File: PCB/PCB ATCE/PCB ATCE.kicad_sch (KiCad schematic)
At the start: 28 parts, among them J1 USB_OTG, J2 Conn_Coaxial, SW1 SW_Push, SW2 SW_Push, U2 ${SIM.PARAMS}, Y1 16MHz

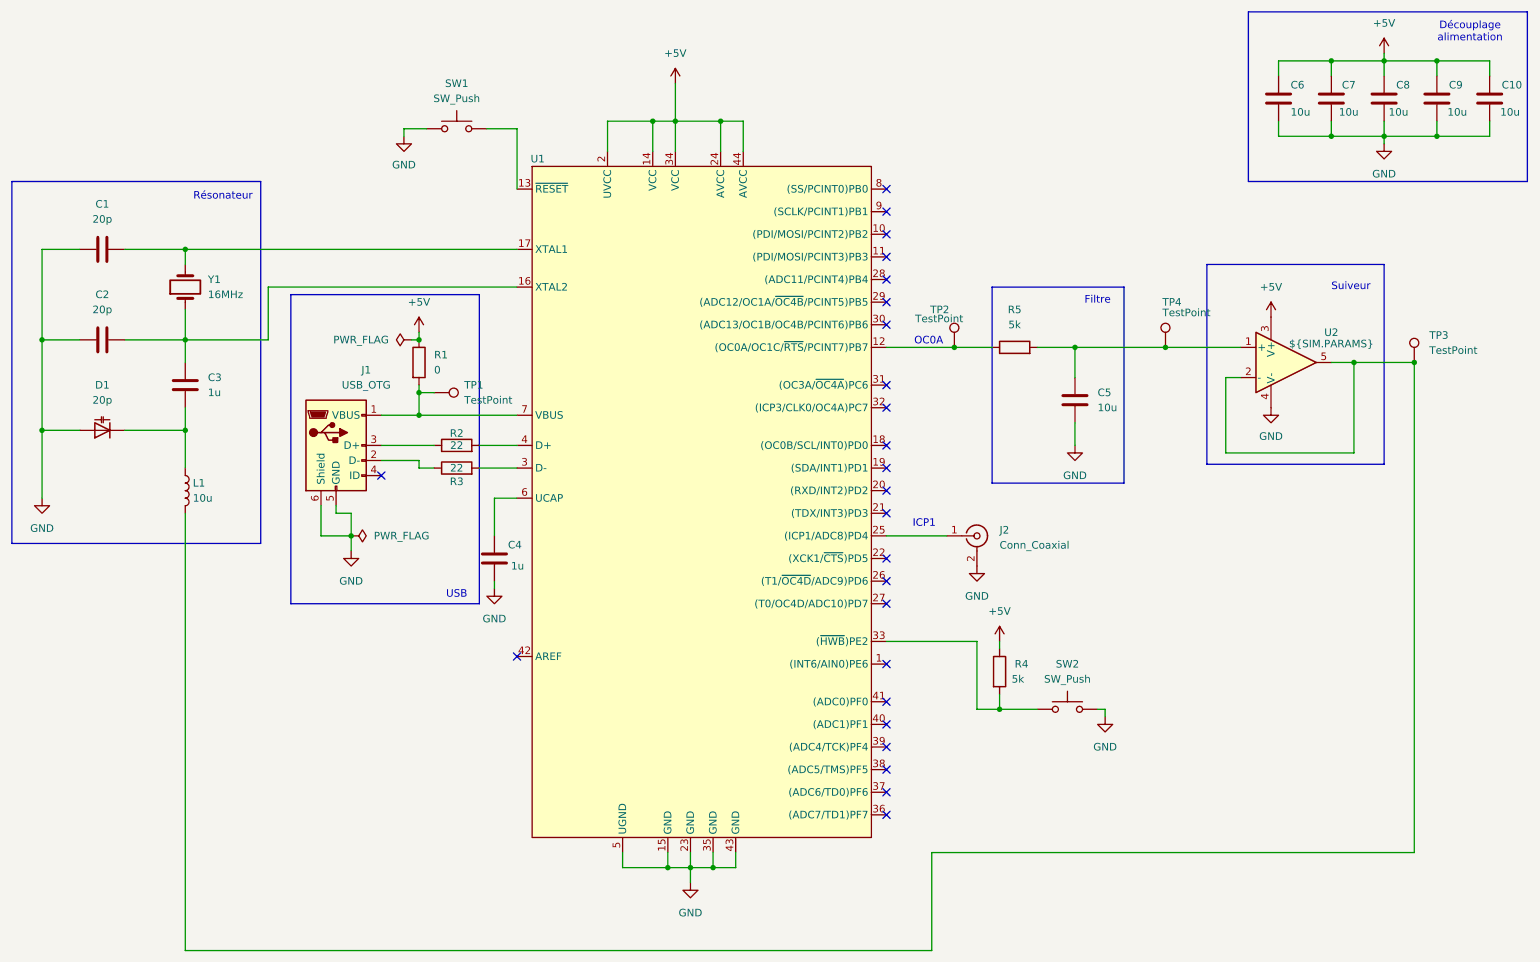
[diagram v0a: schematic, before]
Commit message: Modification des condensateurs de pieds du résonateur et retrait du point de test de l'alimentation
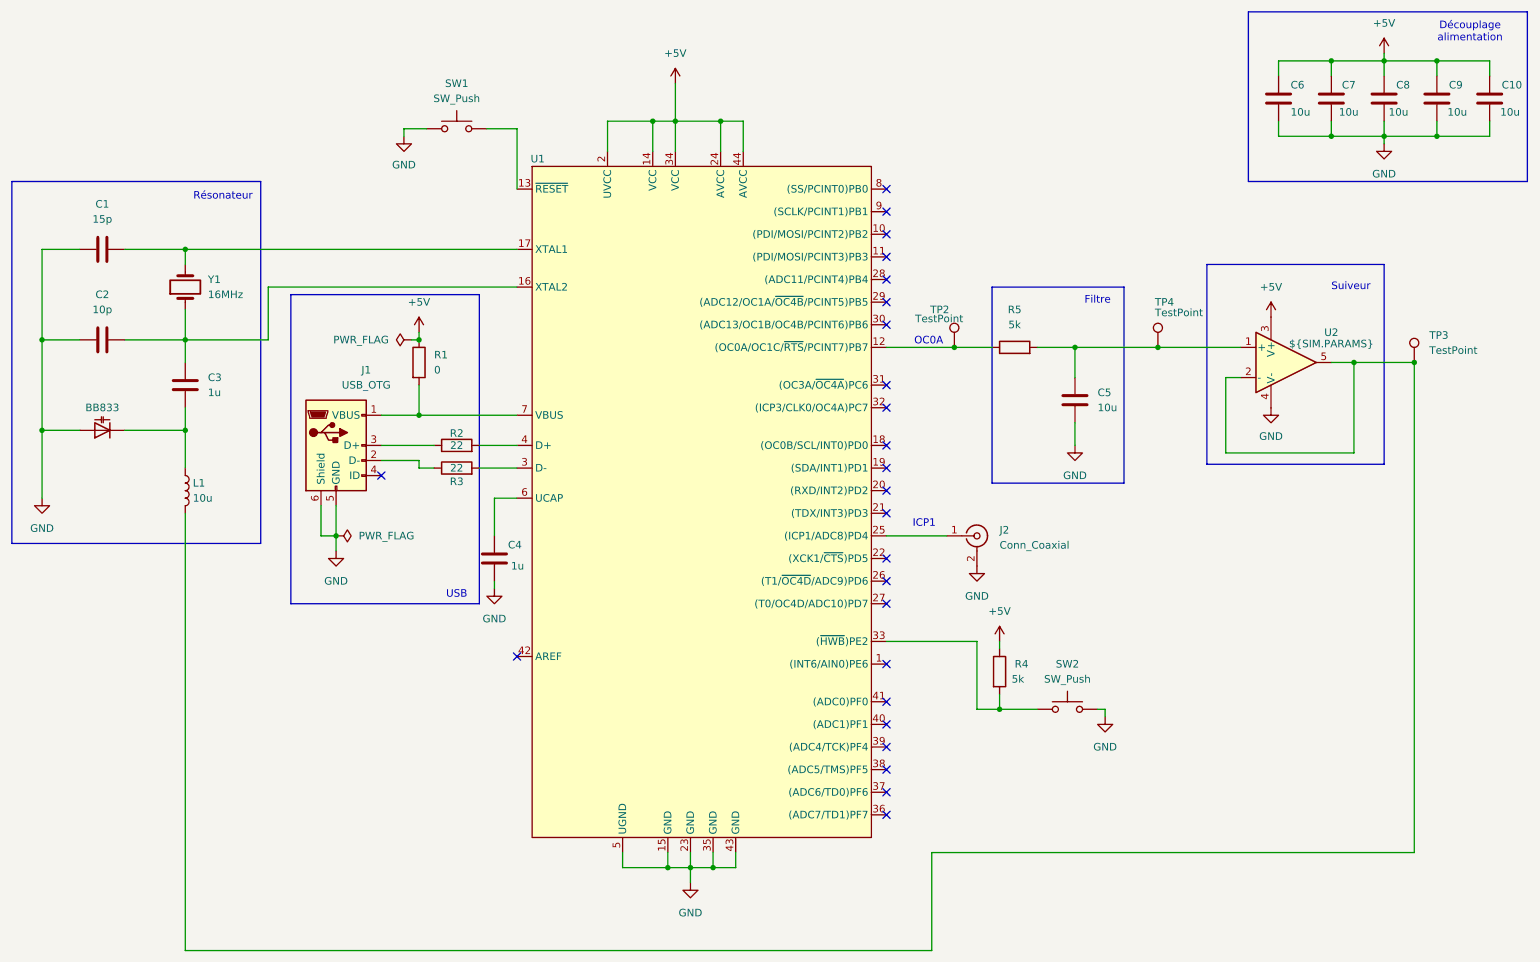
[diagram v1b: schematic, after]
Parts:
- removed TP1: TestPoint, symbol Connector:TestPoint
- BB833: renamed from D1; value 20p -> ~
- C1: value 20p -> 15p
- C2: value 20p -> 10p
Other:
- moved on the sheet: TP4
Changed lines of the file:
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@@
 	)
 	(junction
-		(at 85.09 78.74)
-		(diameter 0)
-		(color 0 0 0 0)
-	)
-	(junction
 		(at 134.62 158.75)
 		(diameter 0)
@@
 	)
 	(junction
-		(at 73.66 102.87)
+		(at 71.12 102.87)
 		(diameter 0)
 		(color 0 0 0 0)
@@
 	)
 	(junction
-		(at 210.82 71.12)
-		(diameter 0)
-		(color 0 0 0 0)
-	)
-	(junction
 		(at 45.72 85.09)
 		(diameter 0)
@@
 	)
 	(junction
+		(at 209.55 71.12)
+		(diameter 0)
+		(color 0 0 0 0)
+	)
+	(junction
 		(at 21.59 85.09)
 		(diameter 0)
@@
 	(wire
 		(pts
+			(xy 71.12 97.79) (xy 71.12 102.87)
+		)
+		(stroke
+			(width 0)
+			(type default)
+		)
+	)
+	(wire
+		(pts
 			(xy 247.65 33.02) (xy 247.65 35.56)
 		)
@@
 	(wire
 		(pts
-			(xy 71.12 99.06) (xy 73.66 99.06)
-		)
-		(stroke
-			(width 0)
-			(type default)
-		)
-	)
-	(wire
-		(pts
 			(xy 138.43 158.75) (xy 138.43 156.21)
 		)
@@
 	(wire
 		(pts
-			(xy 68.58 102.87) (xy 73.66 102.87)
+			(xy 68.58 102.87) (xy 71.12 102.87)
 		)
 		(stroke
@@
 	(wire
 		(pts
-			(xy 85.09 78.74) (xy 85.09 77.47)
-		)
-		(stroke
-			(width 0)
-			(type default)
-		)
-	)
-	(wire
-		(pts
 			(xy 85.09 90.17) (xy 85.09 91.44)
 		)
@@
 	(wire
 		(pts
-			(xy 210.82 71.12) (xy 223.52 71.12)
-		)
-		(stroke
-			(width 0)
-			(type default)
-		)
-	)
-	(wire
-		(pts
-			(xy 71.12 97.79) (xy 71.12 99.06)
-		)
-		(stroke
-			(width 0)
-			(type default)
-		)
-	)
-	(wire
-		(pts
 			(xy 179.07 120.65) (xy 163.83 120.65)
 		)
@@
 	(wire
 		(pts
-			(xy 87.63 78.74) (xy 85.09 78.74)
-		)
-		(stroke
-			(width 0)
-			(type default)
-		)
-	)
-	(wire
-		(pts
 			(xy 45.72 69.85) (xy 45.72 64.77)
 		)
@@
 	(wire
 		(pts
-			(xy 73.66 99.06) (xy 73.66 102.87)
-		)
-		(stroke
-			(width 0)
-			(type default)
-		)
-	)
-	(wire
-		(pts
 			(xy 35.56 54.61) (xy 45.72 54.61)
 		)
@@
 	(wire
 		(pts
-			(xy 195.58 71.12) (xy 210.82 71.12)
+			(xy 195.58 71.12) (xy 209.55 71.12)
 		)
 		(stroke
@@
 	(wire
 		(pts
-			(xy 73.66 102.87) (xy 73.66 105.41)
+			(xy 71.12 102.87) (xy 71.12 105.41)
 		)
 		(stroke
@@
 	(wire
 		(pts
-			(xy 85.09 78.74) (xy 85.09 82.55)
+			(xy 85.09 77.47) (xy 85.09 82.55)
 		)
 		(stroke
@@
 	(wire
 		(pts
+			(xy 209.55 71.12) (xy 223.52 71.12)
+		)
+		(stroke
+			(width 0)
+			(type default)
+		)
+	)
+	(wire
+		(pts
 			(xy 139.7 33.02) (xy 139.7 38.1)
 		)
@@
 			)
 		)
-		(property "Value" "20p"
+		(property "Value" "15p"
 			(at 31.75 49.53 90)
 			(effects
@@
 	(symbol
 		(lib_id "Connector:TestPoint")
-		(at 210.82 71.12 0)
+		(at 209.55 71.12 0)
 		(unit 1)
 		(exclude_from_sim no)
@@
 		(dnp no)
 		(property "Reference" "TP4"
-			(at 210.312 63.5 0)
+			(at 209.042 63.5 0)
 			(effects
 				(font
@@
 		)
 		(property "Value" "TestPoint"
-			(at 210.312 65.278 0)
+			(at 209.042 65.278 0)
 			(effects
 				(font
@@
 		)
 		(property "Footprint" ""
-			(at 215.9 71.12 0)
+			(at 214.63 71.12 0)
 			(effects
 				(font
@@
 		)
 		(property "Datasheet" "~"
-			(at 215.9 71.12 0)
+			(at 214.63 71.12 0)
 			(effects
 				(font
@@
 		)
 		(property "Description" "test point"
-			(at 210.82 71.12 0)
+			(at 209.55 71.12 0)
 			(effects
 				(font
@@
 	)
 	(symbol
-		(lib_id "Connector:TestPoint")
-		(at 87.63 78.74 270)
-		(unit 1)
-		(exclude_from_sim no)
-		(in_bom yes)
-		(on_board yes)
-		(dnp no)
-		(fields_autoplaced yes)
-		(property "Reference" "TP1"
-			(at 92.71 77.4699 90)
-			(effects
-				(font
-					(size 1.27 1.27)
-				)
-				(justify left)
-			)
-		)
-		(property "Value" "TestPoint"
-			(at 92.71 80.0099 90)
-			(effects
-				(font
-					(size 1.27 1.27)
-				)
-				(justify left)
-			)
-		)
-		(property "Footprint" ""
-			(at 87.63 83.82 0)
-			(effects
-				(font
-					(size 1.27 1.27)
-				)
-				(hide yes)
-			)
-		)
-		(property "Datasheet" "~"
-			(at 87.63 83.82 0)
-			(effects
-				(font
-					(size 1.27 1.27)
-				)
-				(hide yes)
-			)
-		)
-		(property "Description" "test point"
-			(at 87.63 78.74 0)
-			(effects
-				(font
-					(size 1.27 1.27)
-				)
-				(hide yes)
-			)
-		)
-		(pin "1"
-		)
-		(instances
-			(project "PCB ATCE"
-				(path "/0ca51401-30cc-4cc1-83e5-abd29d3bd674"
-					(reference "TP1")
-					(unit 1)
-				)
-			)
-		)
-	)
-	(symbol
 		(lib_id "power:+5V")
 		(at 128.27 26.67 0)
@@
 	(symbol
 		(lib_id "power:PWR_FLAG")
-		(at 73.66 102.87 270)
+		(at 71.12 102.87 270)
 		(unit 1)
 		(exclude_from_sim no)
@@
 		(fields_autoplaced yes)
 		(property "Reference" "#FLG01"
-			(at 75.565 102.87 0)
+			(at 73.025 102.87 0)
 			(effects
 				(font
@@
 		)
 		(property "Value" "PWR_FLAG"
-			(at 77.47 102.8699 90)
+			(at 74.93 102.8699 90)
 			(effects
 				(font
@@
 		)
 		(property "Footprint" ""
-			(at 73.66 102.87 0)
+			(at 71.12 102.87 0)
 			(effects
 				(font
@@
 		)
 		(property "Datasheet" "~"
-			(at 73.66 102.87 0)
+			(at 71.12 102.87 0)
 			(effects
 				(font
@@
 		)
 		(property "Description" "Special symbol for telling ERC where power comes from"
-			(at 73.66 102.87 0)
+			(at 71.12 102.87 0)
 			(effects
 				(font
@@
 	(symbol
 		(lib_id "power:GND")
-		(at 73.66 105.41 0)
+		(at 71.12 105.41 0)
 		(unit 1)
 		(exclude_from_sim no)
@@
 		(fields_autoplaced yes)
 		(property "Reference" "#PWR03"
-			(at 73.66 111.76 0)
+			(at 71.12 111.76 0)
 			(effects
 				(font
@@
 		)
 		(property "Value" "GND"
-			(at 73.66 110.49 0)
+			(at 71.12 110.49 0)
 			(effects
 				(font
@@
 		)
 		(property "Footprint" ""
-			(at 73.66 105.41 0)
+			(at 71.12 105.41 0)
 			(effects
 				(font
@@
 		)
 		(property "Datasheet" ""
-			(at 73.66 105.41 0)
+			(at 71.12 105.41 0)
 			(effects
 				(font
@@
 		)
 		(property "Description" "Power symbol creates a global label with name \"GND\" , ground"
-			(at 73.66 105.41 0)
+			(at 71.12 105.41 0)
 			(effects
 				(font
@@
 		(on_board yes)
 		(dnp no)
-		(property "Reference" "D1"
-			(at 31.75 77.47 0)
+		(property "Reference" "BB833"
+			(at 31.75 81.28 0)
 			(effects
 				(font
@@
 			)
 		)
-		(property "Value" "20p"
+		(property "Value" "~"
 			(at 31.75 80.01 0)
 			(effects
@@
 			(project ""
 				(path "/0ca51401-30cc-4cc1-83e5-abd29d3bd674"
-					(reference "D1")
+					(reference "BB833")
 					(unit 1)
 				)
@@
 			)
 		)
-		(property "Value" "20p"
+		(property "Value" "10p"
 			(at 31.75 64.77 90)
 			(effects

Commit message: ajout des empreintes et BOM
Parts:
- BB833: footprint (none) -> Diode_SMD:D_0805_2012Metric_Pad1.15x1.40mm_HandSolder; Prix/U (none) -> 0,172 €
- C1: footprint (none) -> Capacitor_SMD:C_0805_2012Metric_Pad1.18x1.45mm_HandSolder; Prix/U (none) -> 0,0742 €
- C10, C5, C6, C7, C8, C9: footprint (none) -> Capacitor_SMD:C_1206_3216Metric_Pad1.33x1.80mm_HandSolder; Prix/U (none) -> 1,230 €
- C2: footprint (none) -> Capacitor_SMD:C_0805_2012Metric_Pad1.18x1.45mm_HandSolder; Prix/U (none) -> 0,067 €
- C3, C4: footprint (none) -> Capacitor_SMD:C_0805_2012Metric_Pad1.18x1.45mm_HandSolder; Prix/U (none) -> 0,0982 €
- J1: footprint (none) -> Connector_USB:USB_Mini-B_Wuerth_65100516121_Horizontal; Prix/U (none) -> 1,000 €
- J2: footprint (none) -> Connector_Coaxial:SMA_Molex_73251-2200_Horizontal; Prix/U (none) -> 6,940 €
- L1: footprint (none) -> Inductor_SMD:L_0805_2012Metric_Pad1.05x1.20mm_HandSolder; Prix/U (none) -> 0,214 €
- R1, R4: footprint (none) -> Resistor_SMD:R_0805_2012Metric_Pad1.20x1.40mm_HandSolder; Prix/U (none) -> 0,015 €
- R2, R3: footprint (none) -> Resistor_SMD:R_0805_2012Metric_Pad1.20x1.40mm_HandSolder; Prix/U (none) -> 0,016 €
- R5: footprint (none) -> Resistor_SMD:R_0805_2012Metric_Pad1.20x1.40mm_HandSolder; Prix/U (none) -> 0,015€
- SW1, SW2: footprint (none) -> Button_Switch_SMD:SW_Tactile_SPST_NO_Straight_CK_PTS636Sx25SMTRLFS; Prix/U (none) -> 0,937 €
- TP2, TP3, TP4: footprint (none) -> TestPoint:TestPoint_Keystone_5000-5004_Miniature
- U1: footprint (none) -> Package_QFP:TQFP-44_10x10mm_P0.8mm; Prix/U (none) -> 5,250 €
- U2: footprint (none) -> Package_SO:SOIC-8-N7_3.9x4.9mm_P1.27mm; Prix/U (none) -> 0,353 €
- Y1: footprint (none) -> Crystal:Crystal_SMD_Abracon_ABM3-2Pin_5.0x3.2mm_HandSoldering; Prix/U (none) -> 0,258 €

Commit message: PCB
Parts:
- added TP1: TestPoint, TestPoint:TestPoint_Keystone_5000-5004_Miniature, symbol Connector:TestPoint
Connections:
- net GND: now also TP1.1
- net D-: now reaches J1.2 (D-), R3.1
- net D-: now also R3.2, U1.3 (D-)
- net D+: now reaches J1.3 (D+), R2.1
- net D+: now also R2.2, U1.4 (D+)
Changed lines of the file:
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@@
+		)
+	)
+	(label "D-"
+		(at 82.55 90.17 0)
+		(effects
+			(font
+				(size 1.27 1.27)
+			)
+			(justify left bottom)
+		)
+	)
+	(label "D+"
+		(at 99.06 87.63 0)
+		(effects
+			(font
+				(size 1.27 1.27)
+			)
+			(justify left bottom)
+		)
+	)
+	(label "D-"
+		(at 99.06 91.44 0)
+		(effects
+			(font
+				(size 1.27 1.27)
+			)
+			(justify left bottom)
+		)
+	)
+	(label "D+"
+		(at 82.55 87.63 0)
+		(effects
+			(font
+				(size 1.27 1.27)
+			)
+			(justify left bottom)
 		)
 	)
@@
 					(unit 1)
 				)
+			)
+		)
+	)
+	(symbol
+		(lib_id "Connector:TestPoint")
+		(at 134.62 158.75 180)
+		(unit 1)
+		(exclude_from_sim no)
+		(in_bom yes)
+		(on_board yes)
+		(dnp no)
+		(fields_autoplaced yes)
+		(property "Reference" "TP1"
+			(at 137.16 160.7819 0)
+			(effects
+				(font
+					(size 1.27 1.27)
+				)
+				(justify right)
+			)
+		)
+		(property "Value" "TestPoint"
+			(at 137.16 163.3219 0)
+			(effects
+				(font
+					(size 1.27 1.27)
+				)
+				(justify right)
+			)
+		)
+		(property "Footprint" "TestPoint:TestPoint_Keystone_5000-5004_Miniature"
+			(at 129.54 158.75 0)
+			(effects
+				(font
+					(size 1.27 1.27)
+				)
+				(hide yes)
+			)
+		)
+		(property "Datasheet" "~"
+			(at 129.54 158.75 0)
+			(effects
+				(font
+					(size 1.27 1.27)
+				)
+				(hide yes)
+			)
+		)
+		(property "Description" "test point"
+			(at 134.62 158.75 0)
+			(effects
+				(font
+					(size 1.27 1.27)
+				)
+				(hide yes)
+			)
+		)
+		(pin "1"
+		)
+		(instances
+			(project ""
+				(path "/0ca51401-30cc-4cc1-83e5-abd29d3bd674"
+					(reference "TP1")
+					(unit 1)
+				)
